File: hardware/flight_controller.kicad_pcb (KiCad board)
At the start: 6 copper layers, 50 x 50 mm, 81 parts, among them IC2 STM32F722RET6, IC3 W25Q128JVSIQ, J1 Conn_01x03, J2 Conn_01x08, J3 Conn_01x04, J4 Conn_01x04, J5 Conn_01x04, J6 USB4105-GF-A-060, Q1 TPRT9013-33GB, SW2 SW_SPST, U1 BMP581, U2 MP9943GQ-Z, U3 USBLC6-2P6, U4 MP9943GQ-Z, Y2 X322525MOB4SI

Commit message: stackup
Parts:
- moved Y2 0.31 mm to (171.8, 96.1), turned to 135 degrees
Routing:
- net /USB_DN: track 13.3 -> 3.77 mm
- net /USB_DP: track 12.0 -> 3.34 mm
- net GNDREF: vias 17 -> 14
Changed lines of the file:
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@@
 	(footprint "drone_footprints:X322525MOB4SI"
 		(layer "F.Cu")
-		(at 172.132816 96.175748 45)
+		(at 171.825748 96.117184 135)
 		(descr "X322525MOB4SI-2")
 		(tags "Crystal or Oscillator")
 		(property "Reference" "Y2"
-			(at -0.199999 0 45)
+			(at -0.199999 0 135)
 			(layer "F.SilkS")
 			(effects
@@
 		)
 		(property "Value" "X322525MOB4SI"
-			(at -0.199999 0 45)
+			(at -0.199999 0 135)
 			(layer "F.SilkS")
 			(hide yes)
@@
 		)
 		(property "Datasheet" "https://datasheet.lcsc.com/szlcsc/Yangxing-Tech-X322525MOB4SI_C9006.pdf"
-			(at 0 0 45)
+			(at 0 0 135)
 			(layer "F.Fab")
 			(hide yes)
@@
 		)
 		(property "Description" "SMD Crystal Resonators 25MHz +/-10ppm SMD-3225_4P RoHS"
-			(at 0 0 45)
+			(at 0 0 135)
 			(layer "F.Fab")
 			(hide yes)
@@
 		)
 		(property "Height" "0.8"
-			(at 0 0 45)
+			(at 0 0 135)
 			(unlocked yes)
 			(layer "F.Fab")
@@
 		)
 		(property "Manufacturer_Name" "Yangxing Tech"
-			(at 0 0 45)
+			(at 0 0 135)
 			(unlocked yes)
 			(layer "F.Fab")
@@
 		)
 		(property "Manufacturer_Part_Number" "X322525MOB4SI"
-			(at 0 0 45)
+			(at 0 0 135)
 			(unlocked yes)
 			(layer "F.Fab")
@@
 		)
 		(property "Mouser Part Number" ""
-			(at 0 0 45)
+			(at 0 0 135)
 			(unlocked yes)
 			(layer "F.Fab")
@@
 		)
 		(property "Mouser Price/Stock" ""
-			(at 0 0 45)
+			(at 0 0 135)
 			(unlocked yes)
 			(layer "F.Fab")
@@
 		)
 		(property "Arrow Part Number" ""
-			(at 0 0 45)
+			(at 0 0 135)
 			(unlocked yes)
 			(layer "F.Fab")
@@
 		)
 		(property "Arrow Price/Stock" ""
-			(at 0 0 45)
+			(at 0 0 135)
 			(unlocked yes)
 			(layer "F.Fab")
@@
 		(attr smd)
 		(fp_line
-			(start -2.2 0.6)
-			(end -2.2 0.6)
+			(start -2.1 0.6)
+			(end -2.1 0.6)
 			(stroke
 				(width 0.1)
@@
 		)
 		(fp_line
-			(start -2.1 0.6)
-			(end -2.1 0.6)
+			(start -2.2 0.6)
+			(end -2.2 0.6)
 			(stroke
 				(width 0.1)
@@
 		)
 		(fp_arc
-			(start -2.2 0.6)
-			(mid -2.15 0.55)
-			(end -2.1 0.6)
+			(start -2.1 0.6)
+			(mid -2.15 0.65)
+			(end -2.2 0.6)
 			(stroke
 				(width 0.1)
@@
 		)
 		(fp_arc
-			(start -2.1 0.6)
-			(mid -2.15 0.65)
-			(end -2.2 0.6)
+			(start -2.2 0.6)
+			(mid -2.15 0.55)
+			(end -2.1 0.6)
 			(stroke
 				(width 0.1)
@@
 		)
 		(fp_line
-			(start -3.2 -2.45)
-			(end 2.8 -2.450001)
+			(start 2.8 -2.450001)
+			(end 2.8 2.450001)
 			(stroke
 				(width 0.1)
@@
 		)
 		(fp_line
-			(start -3.2 2.45)
-			(end -3.2 -2.45)
+			(start 2.8 2.450001)
+			(end -3.2 2.45)
 			(stroke
 				(width 0.1)
@@
 		)
 		(fp_line
-			(start 2.8 -2.450001)
-			(end 2.8 2.450001)
+			(start -3.2 -2.45)
+			(end 2.8 -2.450001)
 			(stroke
 				(width 0.1)
@@
 		)
 		(fp_line
-			(start 2.8 2.450001)
-			(end -3.2 2.45)
+			(start -3.2 2.45)
+			(end -3.2 -2.45)
 			(stroke
 				(width 0.1)
@@
 		)
 		(fp_line
-			(start -1.6 -1.25)
-			(end 1.6 -1.25)
+			(start 1.6 -1.25)
+			(end 1.6 1.25)
 			(stroke
 				(width 0.2)
@@
 		)
 		(fp_line
-			(start -1.6 1.25)
-			(end -1.6 -1.25)
+			(start 1.6 1.25)
+			(end -1.6 1.25)
 			(stroke
 				(width 0.2)
@@
 		)
 		(fp_line
-			(start 1.6 -1.25)
-			(end 1.6 1.25)
+			(start -1.6 -1.25)
+			(end 1.6 -1.25)
 			(stroke
 				(width 0.2)
@@
 		)
 		(fp_line
-			(start 1.6 1.25)
-			(end -1.6 1.25)
+			(start -1.6 1.25)
+			(end -1.6 -1.25)
 			(stroke
 				(width 0.2)
@@
 		)
 		(fp_text user "${REFERENCE}"
-			(at -0.199999 0 45)
+			(at -0.199999 0 135)
 			(layer "F.Fab")
 			(effects
@@
 		)
 		(pad "1" smd rect
-			(at -1.1 0.85 135)
+			(at -1.1 0.85 225)
 			(size 1.2 1.4)
 			(layers "F.Cu" "F.Mask" "F.Paste")
@@
 		)
 		(pad "2" smd rect
-			(at 1.1 0.85 135)
+			(at 1.1 0.85 225)
 			(size 1.2 1.4)
 			(layers "F.Cu" "F.Mask" "F.Paste")
@@
 		)
 		(pad "3" smd rect
-			(at 1.1 -0.85 135)
+			(at 1.1 -0.85 225)
 			(size 1.2 1.4)
 			(layers "F.Cu" "F.Mask" "F.Paste")
@@
 		)
 		(pad "4" smd rect
-			(at -1.1 -0.85 135)
+			(at -1.1 -0.85 225)
 			(size 1.2 1.4)
 			(layers "F.Cu" "F.Mask" "F.Paste")
@@
 	)
 	(via
-		(at 177.490155 112.591688)
-		(size 0.4)
-		(drill 0.2)
-		(layers "F.Cu" "B.Cu")
-		(free yes)
-		(net 12)
-	)
-	(via
-		(at 169.947186 105.753987)
+		(at 169.603245 106.089198)
 		(size 0.4)
 		(drill 0.2)
@@
 	)
 	(via
-		(at 188.243515 104.325149)
+		(at 188.703833 103.820937)
 		(size 0.4)
 		(drill 0.2)
@@
 	)
 	(via
-		(at 183.55337 117.507527)
-		(size 0.4)
-		(drill 0.2)
-		(layers "F.Cu" "B.Cu")
-		(free yes)
-		(net 12)
-	)
-	(via
 		(at 150.781709 82.359765)
 		(size 0.4)
@@
 	)
 	(via
-		(at 168.957921 101.710651)
-		(size 0.4)
-		(drill 0.2)
-		(layers "F.Cu" "B.Cu")
-		(free yes)
-		(net 12)
-	)
-	(via
 		(at 198.2 82.2)
 		(size 0.4)
@@
 	)
 	(via
-		(at 151.670732 81.421352)
+		(at 179.903619 93.036362)
 		(size 0.4)
 		(drill 0.2)
@@
 	)
 	(via
-		(at 177.027004 93.432097)
+		(at 151.670732 81.421352)
 		(size 0.4)
 		(drill 0.2)
@@
 	)
 	(segment
-		(start 172 95.902925)
-		(end 172 97.510645)
+		(start 171.552925 96.25)
+		(end 173.160645 96.25)
 		(width 0.2)
 		(layer "F.Cu")
@@
 	)
 	(segment
-		(start 172 97.510645)
-		(end 171.956039 97.554606)
+		(start 173.160645 96.25)
+		(end 173.204606 96.293961)
 		(width 0.2)
 		(layer "F.Cu")
@@
 	)
 	(segment
-		(start 171.089354 94.742921)
-		(end 171.089354 94.992279)
+		(start 170.392921 97.160646)
+		(end 170.642279 97.160646)
 		(width 0.2)
 		(layer "F.Cu")
@@
 	)
 	(segment
-		(start 171.089354 94.992279)
-		(end 172 95.902925)
+		(start 170.642279 97.160646)
+		(end 171.552925 96.25)
 		(width 0.2)
 		(layer "F.Cu")
@@
 	)
 	(segment
-		(start 185.025 106.906163)
-		(end 185.025 112.85)
-		(width 0.2)
-		(layer "F.Cu")
-		(net 46)
-	)
-	(segment
 		(start 191.0134 112.25)
 		(end 191.9075 112.25)
@@
 	)
 	(segment
-		(start 183.865551 105.746714)
-		(end 185.025 106.906163)
-		(width 0.2)
-		(layer "F.Cu")
-		(net 46)
-	)
-	(segment
 		(start 183.830197 105.746714)
 		(end 183.865551 105.746714)
@@
 	)
 	(segment
-		(start 185.025 112.85)
-		(end 186.4 114.225)
-		(width 0.2)
-		(layer "F.Cu")
-		(net 46)
-	)
-	(segment
-		(start 185.475 106.719765)
-		(end 185.475 112.538603)
-		(width 0.2)
-		(layer "F.Cu")
-		(net 47)
-	)
-	(segment
 		(start 189.070292 112.875736)
 		(end 189.820564 112.875736)
@@
 		(width 0.2)
 		(layer "F.Cu")
-		(net 47)
-	)
-	(segment
-		(start 184.18375 105.428515)
-		(end 185.475 106.719765)
-		(width 0.2)
-		(layer "F.Cu")
-		(net 47)
-	)
-	(segment
-		(start 185.475 112.538603)
-		(end 185.661397 112.725)
-		(width 0.2)
-		(layer "F.Cu")
-		(net 47)
-	)
-	(segment
-		(start 185.661397 112.725)
-		(end 186.4 112.725)
-		(width 0.2)
-		(layer "F.Cu")

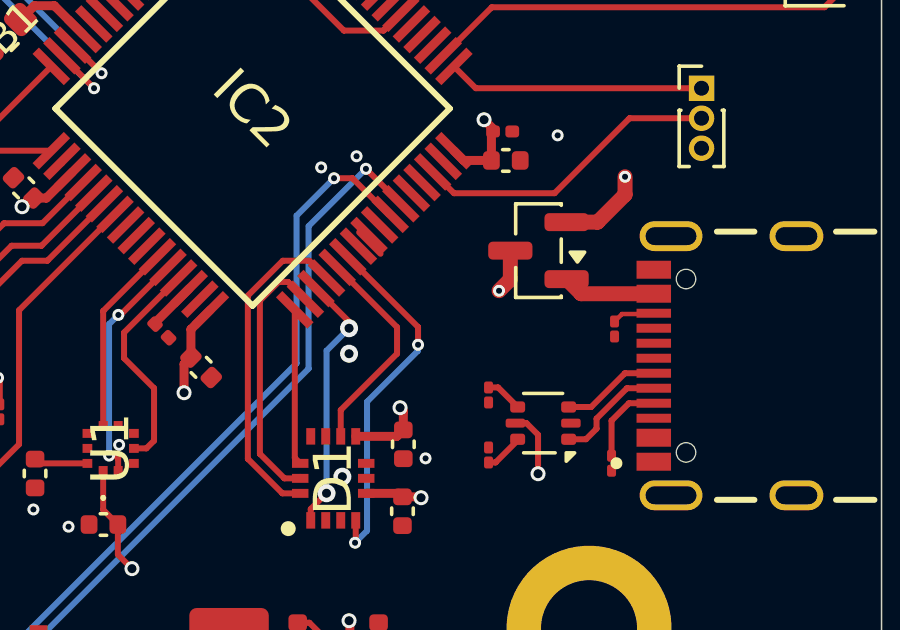
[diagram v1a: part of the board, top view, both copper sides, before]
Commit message: differential pair
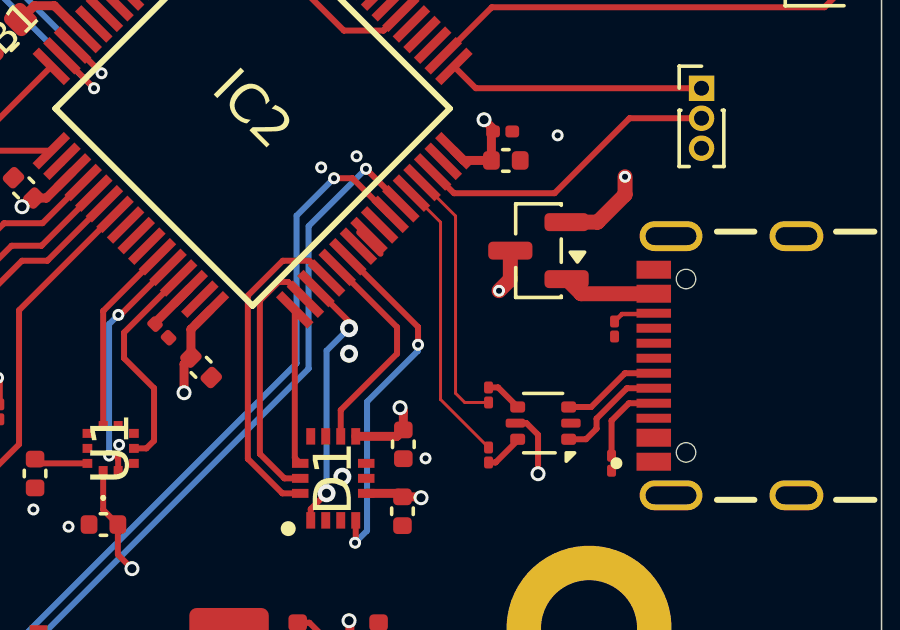
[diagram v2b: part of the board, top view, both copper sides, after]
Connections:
- IC3 pad 8: +3.3v -> +3.3V
- R16 pad 1: +3.3v -> +3.3V
- R17 pad 1: +3.3v -> +3.3V
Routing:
- net /USB_DN: track 3.77 -> 13.3 mm
- net /USB_DP: track 3.34 -> 12.1 mm
- net +3.3V: track 48.4 -> 51.4 mm, vias 13 -> 15
- net +3.3v: track 2.98 -> 0.00 mm, vias 2 -> 0

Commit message: layout
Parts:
- moved C35 0.64 mm to (171.2, 93.0)
- moved Y2 0.34 mm to (172.1, 96.3), turned to -135 degrees
- moved C36 0.22 mm to (169.4, 94.9), turned to 45 degrees
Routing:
- net /HSE_IN: track 11.9 -> 7.12 mm
- net /HSE_OUT: track 11.3 -> 9.59 mm
- net GNDREF: track 0.40 -> 0.46 mm, vias 14 -> 15
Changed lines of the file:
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@@
 	(footprint "Capacitor_SMD:C_0402_1005Metric"
 		(layer "F.Cu")
-		(at 170.61386 93.361869 -135)
+		(at 171.16517 93.04219 -135)
 		(descr "Capacitor SMD 0402 (1005 Metric), square (rectangular) end terminal, IPC-7351 nominal, (Body size source: IPC-SM-782 page 76, https://www.pcb-3d.com/wordpress/wp-content/uploads/ipc-sm-782a_amendment_1_and_2.pdf), generated with kicad-footprint-generator")
 		(tags "capacitor")
@@
 	(footprint "drone_footprints:X322525MOB4SI"
 		(layer "F.Cu")
-		(at 171.825748 96.117184 135)
+		(at 172.13003 96.26123 -135)
 		(descr "X322525MOB4SI-2")
 		(tags "Crystal or Oscillator")
 		(property "Reference" "Y2"
-			(at -0.199999 0 135)
+			(at -0.199999 0 45)
 			(layer "F.SilkS")
 			(effects
@@
 		)
 		(property "Value" "X322525MOB4SI"
-			(at -0.199999 0 135)
+			(at -0.199999 0 45)
 			(layer "F.SilkS")
 			(hide yes)
@@
 		)
 		(property "Datasheet" "https://datasheet.lcsc.com/szlcsc/Yangxing-Tech-X322525MOB4SI_C9006.pdf"
-			(at 0 0 135)
+			(at 0 0 45)
 			(layer "F.Fab")
 			(hide yes)
@@
 		)
 		(property "Description" "SMD Crystal Resonators 25MHz +/-10ppm SMD-3225_4P RoHS"
-			(at 0 0 135)
+			(at 0 0 45)
 			(layer "F.Fab")
 			(hide yes)
@@
 		)
 		(property "Height" "0.8"
-			(at 0 0 135)
+			(at 0 0 225)
 			(unlocked yes)
 			(layer "F.Fab")
@@
 		)
 		(property "Manufacturer_Name" "Yangxing Tech"
-			(at 0 0 135)
+			(at 0 0 225)
 			(unlocked yes)
 			(layer "F.Fab")
@@
 		)
 		(property "Manufacturer_Part_Number" "X322525MOB4SI"
-			(at 0 0 135)
+			(at 0 0 225)
 			(unlocked yes)
 			(layer "F.Fab")
@@
 		)
 		(property "Mouser Part Number" ""
-			(at 0 0 135)
+			(at 0 0 225)
 			(unlocked yes)
 			(layer "F.Fab")
@@
 		)
 		(property "Mouser Price/Stock" ""
-			(at 0 0 135)
+			(at 0 0 225)
 			(unlocked yes)
 			(layer "F.Fab")
@@
 		)
 		(property "Arrow Part Number" ""
-			(at 0 0 135)
+			(at 0 0 225)
 			(unlocked yes)
 			(layer "F.Fab")
@@
 		)
 		(property "Arrow Price/Stock" ""
-			(at 0 0 135)
+			(at 0 0 225)
 			(unlocked yes)
 			(layer "F.Fab")
@@
 		)
 		(fp_line
-			(start 2.8 -2.450001)
-			(end 2.8 2.450001)
+			(start 2.8 2.450001)
+			(end -3.2 2.45)
 			(stroke
 				(width 0.1)
@@
 		)
 		(fp_line
-			(start 2.8 2.450001)
-			(end -3.2 2.45)
+			(start 2.8 -2.450001)
+			(end 2.8 2.450001)
 			(stroke
 				(width 0.1)
@@
 		)
 		(fp_line
-			(start -3.2 -2.45)
-			(end 2.8 -2.450001)
+			(start -3.2 2.45)
+			(end -3.2 -2.45)
 			(stroke
 				(width 0.1)
@@
 		)
 		(fp_line
-			(start -3.2 2.45)
-			(end -3.2 -2.45)
+			(start -3.2 -2.45)
+			(end 2.8 -2.450001)
 			(stroke
 				(width 0.1)
@@
 		)
 		(fp_line
-			(start 1.6 -1.25)
-			(end 1.6 1.25)
+			(start 1.6 1.25)
+			(end -1.6 1.25)
 			(stroke
 				(width 0.2)
@@
 		)
 		(fp_line
-			(start 1.6 1.25)
-			(end -1.6 1.25)
+			(start 1.6 -1.25)
+			(end 1.6 1.25)
 			(stroke
 				(width 0.2)
@@
 		)
 		(fp_line
-			(start -1.6 -1.25)
-			(end 1.6 -1.25)
+			(start -1.6 1.25)
+			(end -1.6 -1.25)
 			(stroke
 				(width 0.2)
@@
 		)
 		(fp_line
-			(start -1.6 1.25)
-			(end -1.6 -1.25)
+			(start -1.6 -1.25)
+			(end 1.6 -1.25)
 			(stroke
 				(width 0.2)
@@
 		)
 		(fp_text user "${REFERENCE}"
-			(at -0.199999 0 135)
+			(at -0.199999 0 45)
 			(layer "F.Fab")
 			(effects
@@
 		)
 		(pad "1" smd rect
-			(at -1.1 0.85 225)
+			(at -1.1 0.85 315)
 			(size 1.2 1.4)
 			(layers "F.Cu" "F.Mask" "F.Paste")
@@
 		)
 		(pad "2" smd rect
-			(at 1.1 0.85 225)
+			(at 1.1 0.85 315)
 			(size 1.2 1.4)
 			(layers "F.Cu" "F.Mask" "F.Paste")
@@
 		)
 		(pad "3" smd rect
-			(at 1.1 -0.85 225)
+			(at 1.1 -0.85 315)
 			(size 1.2 1.4)
 			(layers "F.Cu" "F.Mask" "F.Paste")
@@
 		)
 		(pad "4" smd rect
-			(at -1.1 -0.85 225)
+			(at -1.1 -0.85 315)
 			(size 1.2 1.4)
 			(layers "F.Cu" "F.Mask" "F.Paste")
@@
 	(footprint "Capacitor_SMD:C_0402_1005Metric"
 		(layer "F.Cu")
-		(at 169.185038 94.790691 -135)
+		(at 169.350845 94.932508 45)
 		(descr "Capacitor SMD 0402 (1005 Metric), square (rectangular) end terminal, IPC-7351 nominal, (Body size source: IPC-SM-782 page 76, https://www.pcb-3d.com/wordpress/wp-content/uploads/ipc-sm-782a_amendment_1_and_2.pdf), generated with kicad-footprint-generator")
 		(tags "capacitor")
@@
 		(attr smd)
 		(fp_line
-			(start -0.107836 0.36)
-			(end 0.107836 0.36)
+			(start -0.107836 -0.36)
+			(end 0.107836 -0.36)
 			(stroke
 				(width 0.12)
@@
 		)
 		(fp_line
-			(start -0.107836 -0.36)
-			(end 0.107836 -0.36)
+			(start -0.107836 0.36)
+			(end 0.107836 0.36)
 			(stroke
 				(width 0.12)
@@
 		)
 		(pad "1" smd roundrect
-			(at -0.48 0 225)
+			(at -0.48 0 45)
 			(size 0.56 0.62)
 			(layers "F.Cu" "F.Mask" "F.Paste")
@@
 		)
 		(pad "2" smd roundrect
-			(at 0.48 0 225)
+			(at 0.48 0 45)
 			(size 0.56 0.62)
 			(layers "F.Cu" "F.Mask" "F.Paste")
@@
 	)
 	(segment
+		(start 173.160645 96.25)
+		(end 173.204606 96.293961)
+		(width 0.2)
+		(layer "F.Cu")
+		(net 11)
+	)
+	(segment
 		(start 178.21645 84.96645)
 		(end 178 84.75)
@@
 	)
 	(via
+		(at 174.287852 96.860528)
+		(size 0.4)
+		(drill 0.2)
+		(layers "F.Cu" "B.Cu")
+		(free yes)
+		(net 11)
+	)
+	(via
 		(at 197.224771 128.529174)
 		(size 0.4)
@@
 	)
 	(segment
-		(start 172.504982 93.576651)
-		(end 172.255624 93.576651)
-		(width 0.2)
-		(layer "F.Cu")
-		(net 20)
-	)
-	(segment
-		(start 171.552925 96.25)
-		(end 173.160645 96.25)
+		(start 175.140436 97.056953)
+		(end 175.715439 97.631956)
 		(width 0.2)
 		(layer "F.Cu")
@@
 	)
 	(segment
-		(start 173.160645 96.25)
-		(end 173.204606 96.293961)
+		(start 175.140436 96.300373)
+		(end 175.140436 97.056953)
 		(width 0.2)
 		(layer "F.Cu")
@@
 	)
 	(segment
-		(start 174.731913 96.64843)
-		(end 174.731913 95.803582)
+		(start 172.306807 94.882372)
+		(end 170.825759 93.401324)
 		(width 0.2)
 		(layer "F.Cu")
@@
 	)
 	(segment
-		(start 175.715439 97.631956)
-		(end 174.731913 96.64843)
+		(start 170.825759 93.401324)
+		(end 170.825759 93.381601)
 		(width 0.2)
 		(layer "F.Cu")
@@
 	)
 	(segment
-		(start 171.089354 94.516185)
-		(end 171.089354 94.742921)
+		(start 173.704277 94.864214)
+		(end 175.140436 96.300373)
 		(width 0.2)
 		(layer "F.Cu")
@@
 	)
 	(segment
-		(start 170.392921 97.160646)
-		(end 170.642279 97.160646)
+		(start 172.306807 94.882372)
+		(end 172.324965 94.864214)
 		(width 0.2)
 		(layer "F.Cu")
@@
 	)
 	(segment
-		(start 170.642279 97.160646)
-		(end 171.552925 96.25)
+		(start 172.324965 94.864214)
+		(end 173.704277 94.864214)
 		(width 0.2)
 		(layer "F.Cu")
@@
 	)
 	(segment
-		(start 174.731913 95.803582)
-		(end 172.504982 93.576651)
+		(start 170.733014 96.456165)
+		(end 170.733014 97.835477)
 		(width 0.2)
 		(layer "F.Cu")
-		(net 20)
+		(net 21)
 	)
 	(segment
-		(start 172.255624 93.576651)
-		(end 171.089354 94.742921)
+		(start 171.757864 98.860327)
+		(end 173.018409 98.860327)
 		(width 0.2)
 		(layer "F.Cu")
-		(net 20)
+		(net 21)
 	)
 	(segment
-		(start 170.274449 93.70128)
-		(end 171.089354 94.516185)
+		(start 170.733014 97.835477)
+		(end 171.757864 98.860327)
 		(width 0.2)
 		(layer "F.Cu")
-		(net 20)
+		(net 21)
 	)
 	(segment
-		(start 172.010008 98.774845)
-		(end 171.76065 98.774845)
+		(start 174.776376 97.4)
+		(end 175.361886 97.98551)
 		(width 0.2)
 		(layer "F.Cu")
@@
 	)
 	(segment
-		(start 173.511674 97.273179)
-		(end 172.010008 98.774845)
+		(start 170.751172 96.438007)
+		(end 170.733014 96.456165)
 		(width 0.2)
 		(layer "F.Cu")
@@
 	)
 	(segment
-		(start 175.361886 97.98551)
-		(end 173.511674 96.135298)
+		(start 170.751172 96.438007)
+		(end 170.751172 95.701172)
 		(width 0.2)
 		(layer "F.Cu")
@@
 	)
 	(segment
-		(start 173.511674 95.998971)
-		(end 173.511674 97.273179)
+		(start 169.690256 94.640256)
+		(end 169.690256 94.593097)
 		(width 0.2)
 		(layer "F.Cu")
@@
 	)
 	(segment
-		(start 168.845627 95.859822)
-		(end 168.845627 95.130102)
+		(start 173.018409 98.860327)
+		(end 174.478736 97.4)
 		(width 0.2)
 		(layer "F.Cu")
@@
 	)
 	(segment
-		(start 171.76065 98.774845)
-		(end 168.845627 95.859822)
+		(start 170.751172 95.701172)
+		(end 169.690256 94.640256)
 		(width 0.2)
 		(layer "F.Cu")
@@
 	)
 	(segment
-		(start 173.511674 96.135298)
-		(end 173.511674 95.998971)
+		(start 174.478736 97.4)
+		(end 174.776376 97.4)
 		(width 0.2)
 		(layer "F.Cu")

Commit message: fix errors
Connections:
- IC2 pad 44: /USB_DN -> /USB_D_DN
- IC2 pad 45: /USB_DP -> /USB_D_DP
- R10 pad 2: /USB_DP -> /USB_D_DP
- R9 pad 2: /USB_DN -> /USB_D_DN
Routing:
- net /USB_D_DN: track 0.00 -> 9.58 mm
- net /USB_DN: track 13.3 -> 3.74 mm
- net /USB_D_DP: track 0.00 -> 8.75 mm
- net /USB_DP: track 12.1 -> 3.30 mm

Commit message: fix errors
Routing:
- net VBUS: track 3.11 -> 9.59 mm
- net GNDREF: track 0.46 -> 3.18 mm
- net /ESC_USART_RX: track 19.2 -> 20.0 mm
- net /BOOT: vias 3 -> 4

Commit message: fix errors
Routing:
- net /USB_DN: track 3.74 -> 6.27 mm
- net /USB_DP: track 3.30 -> 5.13 mm
- net VBUS: track 9.59 -> 10.1 mm
- net Net-(U4-FB): vias 4 -> 2
- net Net-(U2-FB): vias 3 -> 2
- net GNDREF: vias 15 -> 34
- net /VTX_TX: vias 3 -> 1
- net /ICM_MISO: vias 4 -> 2
- net /FLASH_SCLK: vias 4 -> 2
- net /BOOT: vias 4 -> 2
- net /BMP_SCLK: vias 3 -> 2
